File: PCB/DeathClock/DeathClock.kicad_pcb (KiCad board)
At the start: 2 copper layers, 37.2 x 31.2 mm, 31 parts, among them J1 Conn_01x05_Female, J2 EDP_24pin_conn FFC2B35-24-T, Q1 PJA3431_R1_00001, Q2 PJA3430_R1_00001, U1 STM32L010F4P6, Y1 Crystal

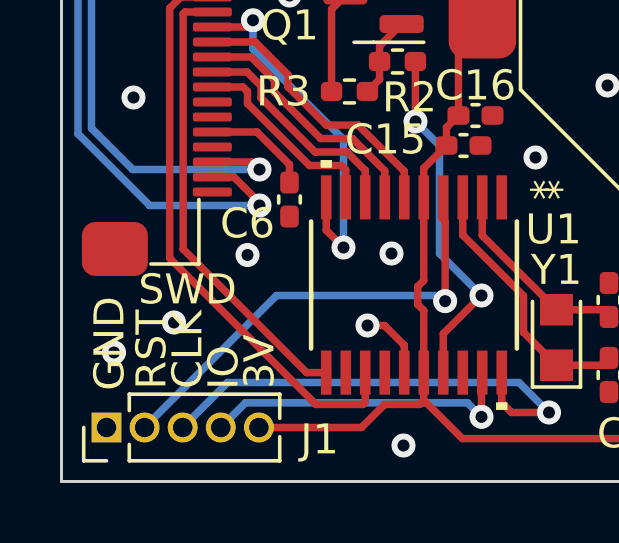
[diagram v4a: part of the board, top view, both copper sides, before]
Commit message: moved text around a bit and added snail
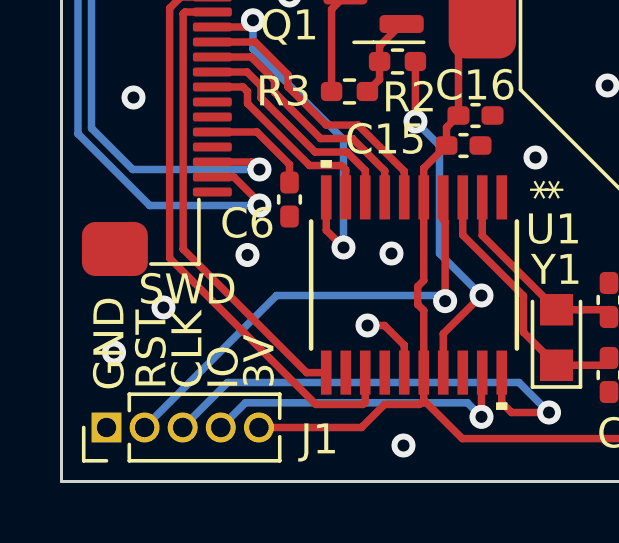
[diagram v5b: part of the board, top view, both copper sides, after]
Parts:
- added G***: LOGO, LOGO, B.Cu at (122.0, 96.6)
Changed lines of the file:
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@@
   (setup
     (stackup
-      (layer "F.SilkS" (type "Top Silk Screen") (color "White"))
+      (layer "F.SilkS" (type "Top Silk Screen") (color "Black"))
       (layer "F.Paste" (type "Top Solder Paste"))
-      (layer "F.Mask" (type "Top Solder Mask") (color "Black") (thickness 0.01))
+      (layer "F.Mask" (type "Top Solder Mask") (color "White") (thickness 0.01))
       (layer "F.Cu" (type "copper") (thickness 0.035))
       (layer "dielectric 1" (type "core") (thickness 0.91) (material "FR4") (epsilon_r 4.5) (loss_tangent 0.02))
       (layer "B.Cu" (type "copper") (thickness 0.035))
-      (layer "B.Mask" (type "Bottom Solder Mask") (color "Black") (thickness 0.01))
+      (layer "B.Mask" (type "Bottom Solder Mask") (color "White") (thickness 0.01))
       (layer "B.Paste" (type "Bottom Solder Paste"))
-      (layer "B.SilkS" (type "Bottom Silk Screen") (color "White"))
+      (layer "B.SilkS" (type "Bottom Silk Screen") (color "Black"))
       (copper_finish "None")
       (dielectric_constraints no)
@@
     )
   )
-  (gr_line (start 137.4 82) (end 138.8 79.2) (layer "B.SilkS") (width 0.15))
-  (gr_line (start 138.8 79.2) (end 140.2 82) (layer "B.SilkS") (width 0.15))
+  (footprint "LOGO" (layer "B.Cu")
+    (at 122 96.6 180)
+    (attr board_only exclude_from_pos_files exclude_from_bom)
+    (fp_text reference "G***" (at 0 0) (layer "B.SilkS") hide
+      (effects (font (size 1.524 1.524) (thickness 0.3)) (justify mirror))
+    )
+    (fp_text value "LOGO" (at 0.75 0) (layer "B.SilkS") hide
+      (effects (font (size 1.524 1.524) (thickness 0.3)) (justify mirror))
+    )
+    (fp_poly (pts
+        (xy -1.430986 0.983803)
+        (xy -1.520422 0.894367)
+        (xy -1.609859 0.983803)
+        (xy -1.520422 1.07324)
+      ) (layer "B.SilkS") (width 0) (fill solid))
+    (fp_poly (pts
+        (xy 0.742425 0.949256)
+        (xy 1.200018 0.629217)
+        (xy 1.423347 0.190996)
+        (xy 1.430986 0.091735)
+        (xy 1.544304 -0.270412)
+        (xy 1.81944 -0.390024)
+        (xy 2.161424 -0.526783)
+        (xy 2.281529 -0.670774)
+        (xy 2.22691 -0.771828)
+        (xy 1.955753 -0.839425)
+        (xy 1.425074 -0.878424)
+        (xy 0.591892 -0.893685)
+        (xy 0.303788 -0.894366)
+        (xy -0.582677 -0.890459)
+        (xy -1.181115 -0.870271)
+        (xy -1.561226 -0.821103)
+        (xy -1.792713 -0.730256)
+        (xy -1.945276 -0.585031)
+        (xy -2.025677 -0.469948)
+        (xy -2.203388 -0.002411)
+        (xy -2.202882 0.055513)
+        (xy -2.107702 0.055513)
+        (xy -1.973663 -0.280722)
+        (xy -1.94906 -0.320972)
+        (xy -1.791163 -0.499599)
+        (xy -1.537008 -0.608492)
+        (xy -1.104939 -0.665215)
+        (xy -0.413301 -0.687331)
+        (xy -0.23737 -0.689141)
+        (xy 1.252113 -0.701502)
+        (xy 1.252113 -0.662316)
+        (xy 1.542671 -0.662316)
+        (xy 1.788733 -0.687249)
+        (xy 2.042667 -0.659139)
+        (xy 2.012324 -0.597028)
+        (xy 1.646109 -0.573403)
+        (xy 1.565141 -0.597028)
+        (xy 1.542671 -0.662316)
+        (xy 1.252113 -0.662316)
+        (xy 1.252113 -0.111153)
+        (xy 1.178049 0.358879)
+        (xy 0.901928 0.63398)
+        (xy 0.796513 0.686781)
+        (xy 0.326798 0.845026)
+        (xy -0.004293 0.894367)
+        (xy -0.36413 0.741666)
+        (xy -0.676131 0.379922)
+        (xy -0.84074 -0.046327)
+        (xy -0.820895 -0.291204)
+        (xy -0.768127 -0.480337)
+        (xy -0.882947 -0.45145)
+        (xy -1.114256 -0.290057)
+        (xy -1.651582 0.051824)
+        (xy -1.991536 0.166688)
+        (xy -2.107702 0.055513)
+        (xy -2.202882 0.055513)
+        (xy -2.200306 0.350103)
+        (xy -2.091259 0.604824)
+        (xy -1.958156 0.530003)
+        (xy -1.942789 0.507023)
+        (xy -1.781057 0.358231)
+        (xy -1.634675 0.507023)
+        (xy -1.497032 0.606755)
+        (xy -1.382373 0.381386)
+        (xy -1.367339 0.32815)
+        (xy -1.28451 0.078635)
+        (xy -1.176319 0.054298)
+        (xy -0.964571 0.277431)
+        (xy -0.792938 0.491902)
+        (xy -0.304308 0.945365)
+        (xy 0.152038 1.07324)
+      ) (layer "B.SilkS") (width 0) (fill solid))
+    (fp_poly (pts
+        (xy 0.57527 0.398272)
+        (xy 0.801037 0.070141)
+        (xy 0.788879 -0.245638)
+        (xy 0.516547 -0.473655)
+        (xy 0.115018 -0.515456)
+        (xy -0.447183 -0.494293)
+        (xy 0.089437 -0.379544)
+        (xy 0.473132 -0.220176)
+        (xy 0.626057 -0.000693)
+        (xy 0.484672 0.243236)
+        (xy 0.166866 0.332591)
+        (xy -0.167843 0.235786)
+        (xy -0.242591 0.171314)
+        (xy -0.327052 0.023286)
+        (xy -0.121612 0.03076)
+        (xy -0.044718 0.048356)
+        (xy 0.264196 0.06433)
+        (xy 0.357747 -0.016746)
+        (xy 0.215038 -0.144697)
+        (xy -0.090517 -0.173888)
+        (xy -0.37506 -0.093758)
+        (xy -0.415819 -0.061176)
+        (xy -0.431675 0.150331)
+        (xy -0.227271 0.383957)
+        (xy 0.085992 0.52772)
+        (xy 0.178874 0.53662)
+      ) (layer "B.SilkS") (width 0) (fill solid))
+    (fp_poly (pts
+        (xy -1.967605 0.983803)
+        (xy -2.057042 0.894367)
+        (xy -2.146479 0.983803)
+        (xy -2.057042 1.07324)
+      ) (layer "B.SilkS") (width 0) (fill solid))
+  )
+  (gr_line (start 138 82) (end 139.4 79.2) (layer "B.SilkS") (width 0.15))
+  (gr_line (start 139.4 79.2) (end 140.8 82) (layer "B.SilkS") (width 0.15))
   (gr_line (start 118.4 77.8) (end 119.4 77.8) (layer "B.SilkS") (width 0.15))
   (gr_line (start 126 99.2) (end 126.4 98.8) (layer "B.SilkS") (width 0.15))
@@
   (gr_line (start 120 85.4) (end 120.4 85.8) (layer "B.SilkS") (width 0.15))
   (gr_line (start 119.4 77.8) (end 119.4 93) (layer "B.SilkS") (width 0.15))
-  (gr_line (start 138.8 80.2) (end 138.8 81.2) (layer "B.SilkS") (width 0.15))
-  (gr_line (start 140.2 82) (end 137.4 82) (layer "B.SilkS") (width 0.15))
+  (gr_line (start 139.4 80.2) (end 139.4 81.2) (layer "B.SilkS") (width 0.15))
+  (gr_line (start 140.8 82) (end 138 82) (layer "B.SilkS") (width 0.15))
   (gr_line (start 120 85.4) (end 120.4 85) (layer "B.SilkS") (width 0.15))
-  (gr_rect (start 144.4 82.4) (end 132.8 89.2) (layer "B.SilkS") (width 0.15) (fill none))
+  (gr_rect (start 145.2 82.4) (end 133.6 89.2) (layer "B.SilkS") (width 0.15) (fill none))
   (gr_rect (start 118.6 100.2) (end 125.4 97.8) (layer "B.SilkS") (width 0.15) (fill none))
-  (gr_line (start 138.8 81.6) (end 138.8 81.6) (layer "B.SilkS") (width 0.15))
+  (gr_line (start 139.4 81.6) (end 139.4 81.6) (layer "B.SilkS") (width 0.15))
   (gr_line (start 119.4 93) (end 118.4 93) (layer "B.SilkS") (width 0.15))
   (gr_rect (start 118 69.6) (end 155.2 100.8) (layer "Edge.Cuts") (width 0.1) (fill none))
@@
     (effects (font (size 1 1) (thickness 0.15)) (justify mirror))
   )
-  (gr_text "Connect flat\ncable before\nputting double\nsided tape" (at 138.6 85.8) (layer "B.SilkS")
+  (gr_text "Connect flat\ncable before\nputting double\nsided tape" (at 139.4 85.8) (layer "B.SilkS")
     (effects (font (size 1 1) (thickness 0.15)) (justify mirror))
   )
@@
   (via (at 133.4 80.8) (size 0.8) (drill 0.4) (layers "F.Cu" "B.Cu") (net 4))
   (via (at 128.2 95.6) (size 0.8) (drill 0.4) (layers "F.Cu" "B.Cu") (net 4))
-  (via (at 121.75 95.5) (size 0.8) (drill 0.4) (layers "F.Cu" "B.Cu") (net 4))
+  (via (at 121.4 95) (size 0.8) (drill 0.4) (layers "F.Cu" "B.Cu") (net 4))
   (via (at 127.6 81.8) (size 0.8) (drill 0.4) (layers "F.Cu" "B.Cu") (free) (net 4))
   (via (at 141.4 85.4) (size 0.8) (drill 0.4) (layers "F.Cu" "B.Cu") (net 4))
